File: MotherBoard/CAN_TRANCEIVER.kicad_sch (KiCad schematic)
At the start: 36 parts, among them U601 PTCAN1462DRQ1, U602 PTCAN1462DRQ1

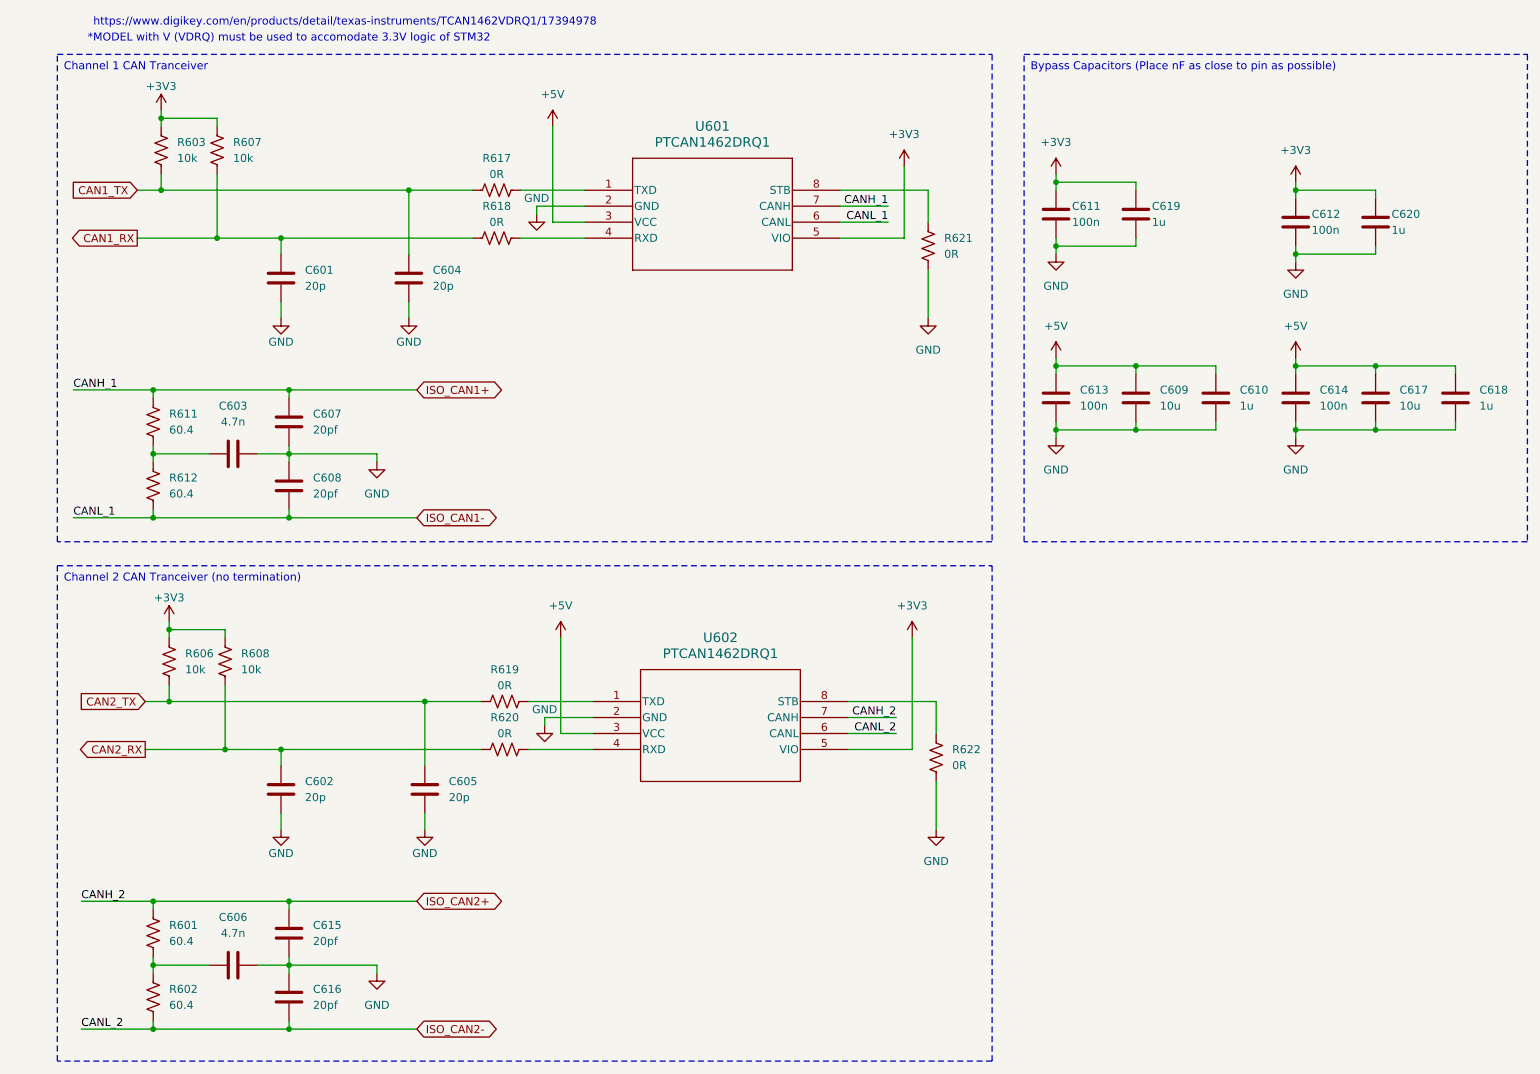
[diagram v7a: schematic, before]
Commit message: BOM completed + All 3D models added + Initial board shape complete
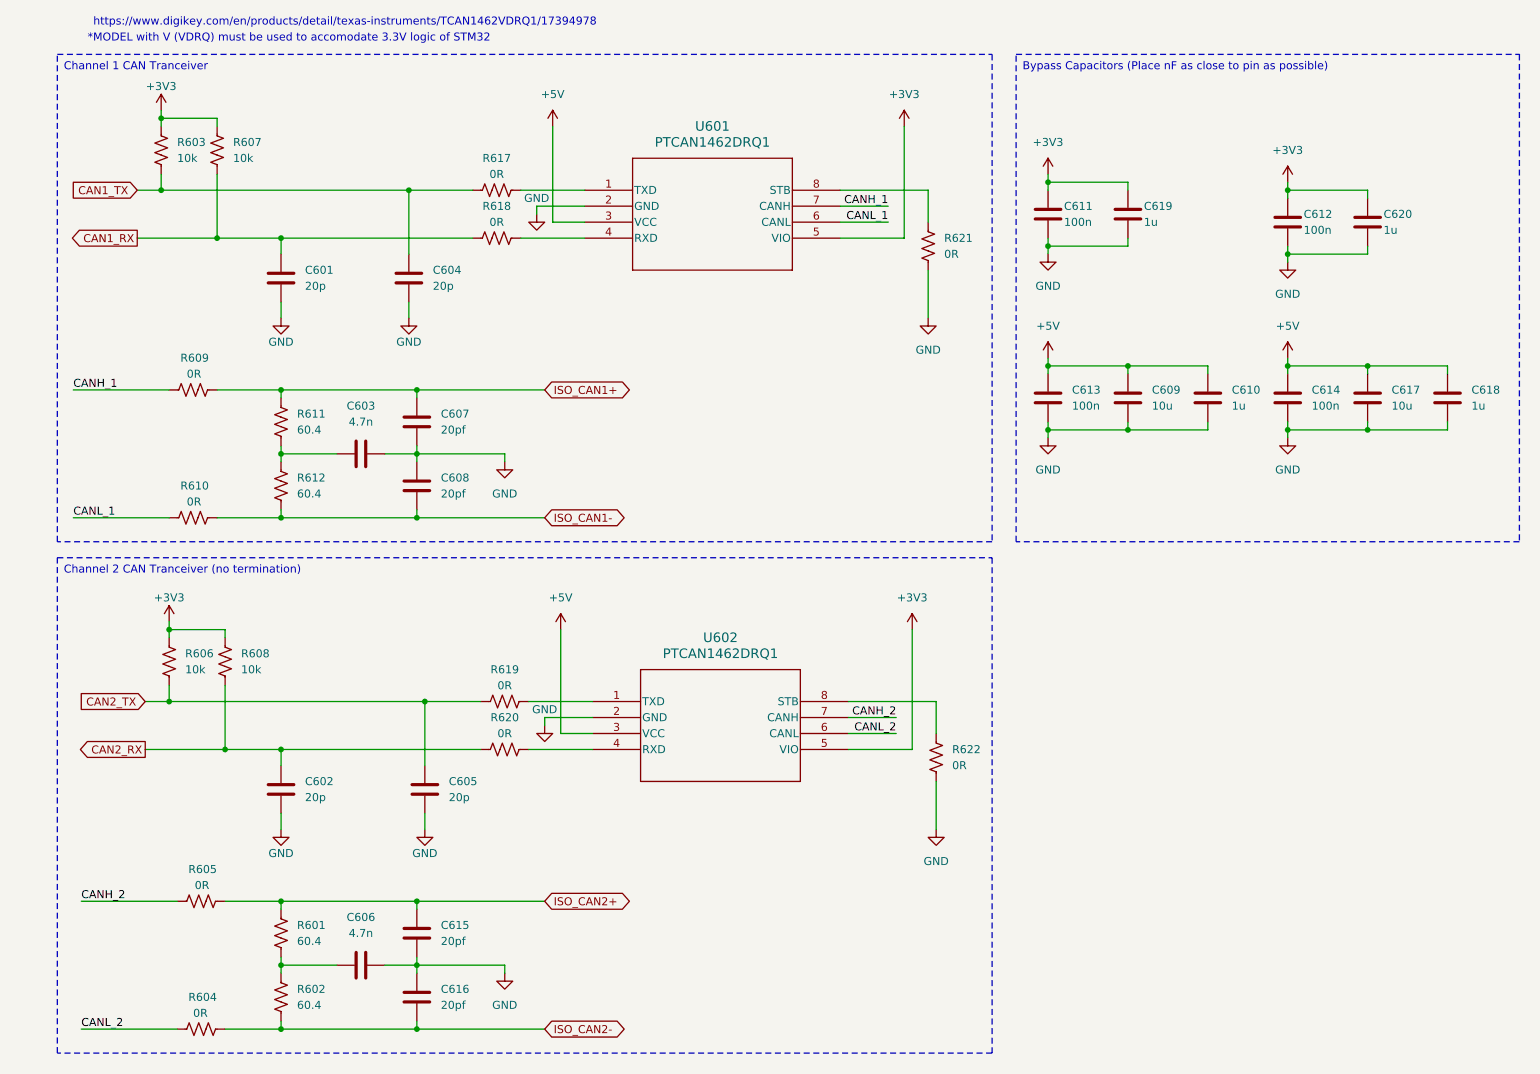
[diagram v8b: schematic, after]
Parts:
- added R604, R605, R609, R610: 0R, Resistor_SMD:R_0805_2012Metric, symbol Device:R_US
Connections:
- net ISO_CAN1+: now also R609.2; no longer U601.7 (CANH)
- net ISO_CAN1-: now also R610.2; no longer U601.6 (CANL)
- net ISO_CAN2+: now also R605.2; no longer U602.7 (CANH)
- net ISO_CAN2-: now also R604.2; no longer U602.6 (CANL)
- new net CANH_1: R609.1, U601.7 (CANH)
- new net CANH_2: R605.1, U602.7 (CANH)
- new net CANL_1: R610.1, U601.6 (CANL)
- new net CANL_2: R604.1, U602.6 (CANL)
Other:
- moved on the sheet: C603, C606, C607, C608, C609, C610, C611, C612, C613, C614, C615, C616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
